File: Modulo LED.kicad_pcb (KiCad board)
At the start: 2 copper layers, 25 x 24 mm, 4 parts, among them J1 Conn_01x02_Pin

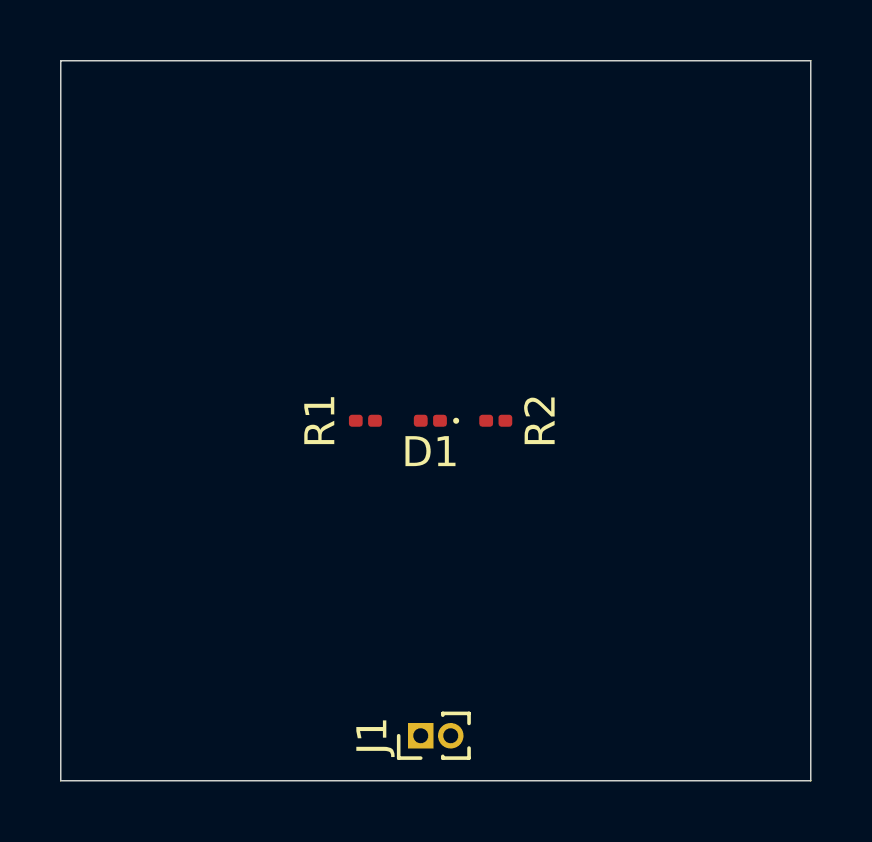
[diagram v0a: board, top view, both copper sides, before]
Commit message: Added filters and overvoltage protecion circuit
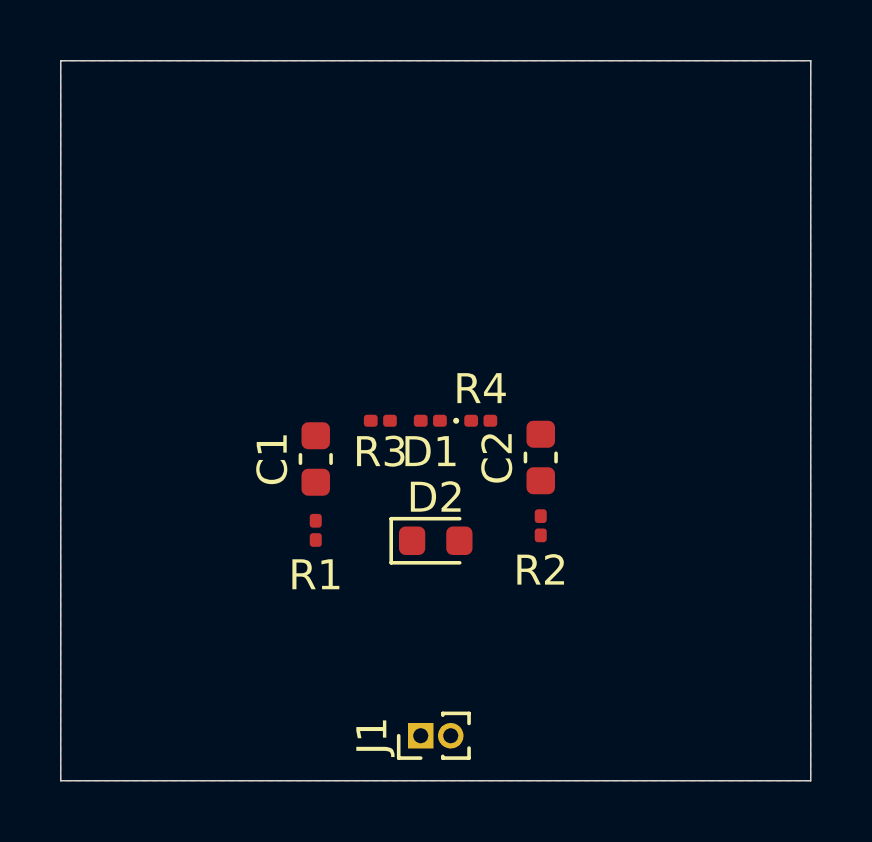
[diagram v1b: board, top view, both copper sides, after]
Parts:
- added C1: C, Capacitor_SMD:C_0603_1608Metric, F.Cu at (141.0, 97.3)
- added C2: C, Capacitor_SMD:C_0603_1608Metric, F.Cu at (148.5, 97.2)
- added D2: D_Zener, Diode_SMD:D_0603_1608Metric, F.Cu at (145.0, 100.0)
- added R3: R, Resistor_SMD:R_0201_0603Metric, F.Cu at (143.2, 96.0)
- added R4: R, Resistor_SMD:R_0201_0603Metric, F.Cu at (146.5, 96.0)
- moved R1 4.01 mm to (141.0, 99.7), turned to -90 degrees
- moved R2 3.81 mm to (148.5, 99.5), turned to -90 degrees
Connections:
- R1 pad 1: Net-(D1-A) -> Net-(C1-Pad1)
- R2 pad 1: Net-(D1-K) -> Net-(C2-Pad1)
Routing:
- added copper zone on F.Cu, net GND
